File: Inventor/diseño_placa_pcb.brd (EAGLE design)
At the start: 100 x 80 mm, 14 parts, among them IC2 7805T

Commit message: pcb_design
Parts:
- removed JP1, JP3, JP4, JP5, JP6: (no value), jumper:JP1
- added VCC1: (no value), con-wago-500:W237-102
- moved X3 81.3 mm to (91.4, 64.8)
- moved X4 78.7 mm to (91.4, 54.6)
- moved VCC 77.8 mm to (88.9, 39.4)
- moved X1 77.6 mm to (12.7, 66.0), turned to 270 degrees
- moved X2 74.9 mm to (12.7, 55.9), turned to 270 degrees
- moved IC2 12.8 mm to (17.8, 21.6), turned to 0 degrees
- moved LEFT_MOTOR 10.5 mm to (34.3, 59.7)
- moved U$1 10.5 mm to (62.2, 16.5), turned to 0 degrees
- moved RIGHT_MOTOR 10.2 mm to (69.8, 59.7)
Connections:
- net N$15 renamed 3.3
- net N$16 renamed 1B_LEFT
- net N$17 renamed 1A_LEFT
- net N$18 renamed 2A_LEFT
- net N$19 renamed 2B_LEFT
- removed net N$6: IC2.2, LEFT_MOTOR.15, LEFT_MOTOR.9, RIGHT_MOTOR.15, RIGHT_MOTOR.9, U$1.GND@1, VCC.2
- new net DIR_RIGHT: RIGHT_MOTOR.8
- new net GND: RIGHT_MOTOR.15, RIGHT_MOTOR.9, U$1.GND@2, VCC.2
- new net N$20: LEFT_MOTOR.8, U$1.D14
- new net N$21: IC2.1, LEFT_MOTOR.16, VCC1.1
- new net S$1: IC2.2, LEFT_MOTOR.15, LEFT_MOTOR.9, VCC1.2
- new net STEP_RIGHT: RIGHT_MOTOR.7
- net N$10: no longer IC2.1, LEFT_MOTOR.16
- net N$12: now also LEFT_MOTOR.1
- net N$14: now also LEFT_MOTOR.7, U$1.D27; no longer LEFT_MOTOR.1
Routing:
- net N$6: track 208.3 -> 0.00 mm
- net N$2: track 141.8 -> 16.4 mm
- net GND: track 0.00 -> 114.8 mm
- net N$5: track 125.2 -> 16.1 mm
- net N$3: track 123.9 -> 15.3 mm
- net 2A_LEFT: track 120.7 -> 16.6 mm
- net 2B_LEFT: track 110.1 -> 17.9 mm
- net S$1: track 0.00 -> 84.1 mm
- net N$4: track 79.9 -> 14.5 mm
- net 1B_LEFT: track 76.5 -> 18.9 mm
- net STEP_RIGHT: track 0.00 -> 57.6 mm
- net DIR_RIGHT: track 0.00 -> 55.0 mm
- net N$21: track 0.00 -> 55.0 mm
- net 1A_LEFT: track 72.1 -> 17.6 mm
- net N$20: track 0.00 -> 52.3 mm
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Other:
- board text added: "GND"
- board text added: "V3.3"
- board text added: "VIN"
- board text added: "VMOT"
- board text added: "vcc"

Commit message: pcb
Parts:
- added U$2: HR911105A, HR911105A:RJ45
- moved U$1 14.5 mm to (48.3, 20.3)
- moved IC2 7.73 mm to (10.2, 22.9)
- moved X2 4.58 mm to (10.2, 52.1)
- moved VCC1 3.81 mm to (10.2, 40.6)
- moved X1 3.59 mm to (10.2, 63.5)
- moved VCC 2.84 mm to (91.4, 38.1)
- moved RIGHT_MOTOR 1.27 mm to (71.1, 59.7)
- moved X3 1.27 mm to (91.4, 66.0)
- moved X4 1.27 mm to (91.4, 53.3)
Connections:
- net 1A_LEFT renamed N$17
- net 1B_LEFT renamed N$16
- net 2A_LEFT renamed N$18
- net 2B_LEFT renamed N$19
- net 3.3 renamed N$15
- net GND renamed N$22
- removed net DIR_RIGHT: RIGHT_MOTOR.8
- removed net S$1: IC2.2, LEFT_MOTOR.15, LEFT_MOTOR.9, VCC1.2
- removed net STEP_RIGHT: RIGHT_MOTOR.7
- new net N$23: U$1.D16, U$2.RD-
- new net N$24: IC2.2, LEFT_MOTOR.15, LEFT_MOTOR.9, U$2.GND, VCC1.2
- new net N$25: U$1.D17, U$2.RD+
- new net N$26: U$1.D5, U$2.P5
- new net N$28: U$1.D18, U$2.P4
- new net N$29: U$1.D21, U$2.TD-
- new net N$30: U$1.D22, U$2.TD+
- new net N$6: RIGHT_MOTOR.8, U$1.D2
- new net N$9: RIGHT_MOTOR.7, U$1.D4
- net N$1: now also U$1.D34
- net N$13: now also U$2.NC
- net N$27: now also U$1.D35
- net N$7: now also U$1.D32
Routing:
- net N$24: track 0.00 -> 167.0 mm
- net N$13: track 32.9 -> 124.2 mm
- net N$9: track 0.00 -> 90.1 mm
- net N$6: track 0.00 -> 90.0 mm
- net N$15: track 149.9 -> 235.7 mm
- net S$1: track 84.1 -> 0.00 mm
- net STEP_RIGHT: track 57.6 -> 0.00 mm
- net DIR_RIGHT: track 55.0 -> 0.00 mm
- net N$27: track 30.4 -> 78.4 mm
- net N$7: track 33.6 -> 78.1 mm
- net N$25: track 0.00 -> 39.0 mm
- net N$23: track 0.00 -> 38.9 mm
- net N$26: track 0.00 -> 35.8 mm
- net N$1: track 23.9 -> 59.4 mm
- net N$28: track 0.00 -> 30.2 mm
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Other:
- board text removed: "GND"
- board text removed: "V3.3"
- board text removed: "VIN"
- board text removed: "VMOT"
- board text removed: "vcc"

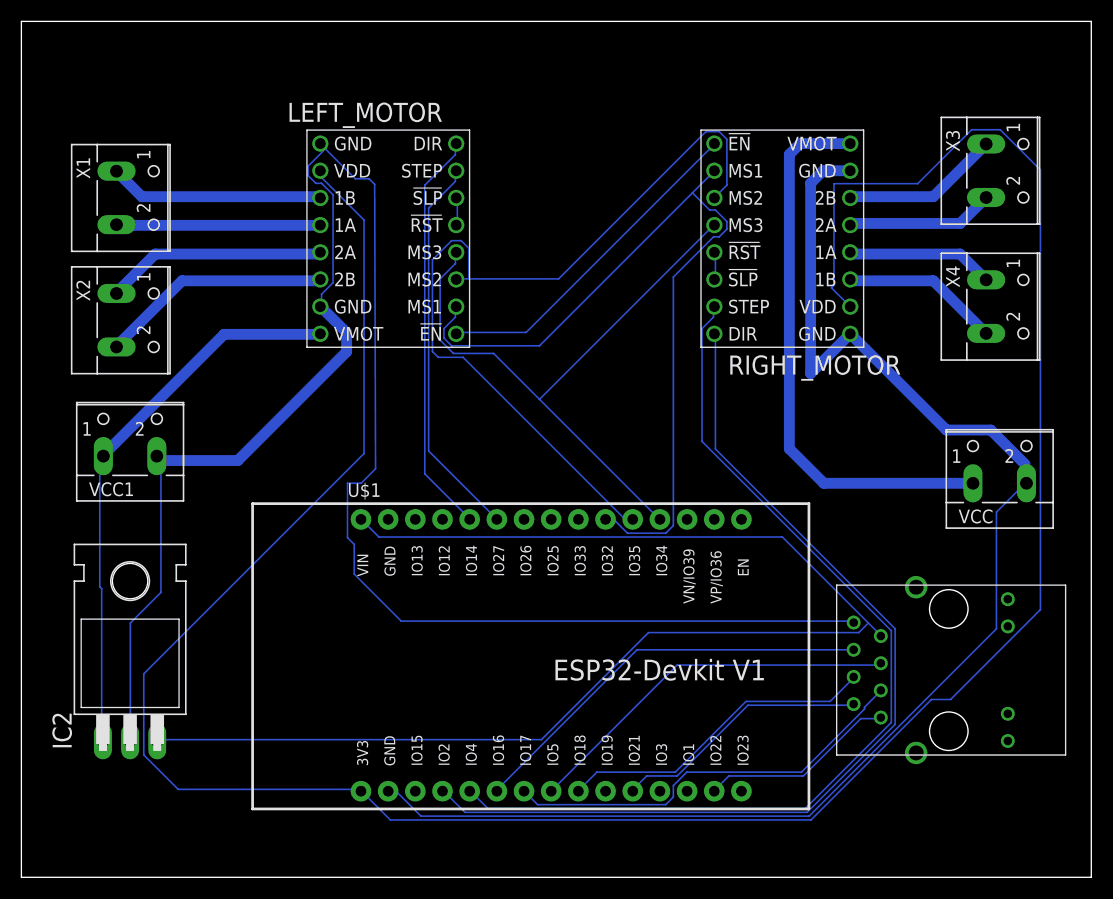
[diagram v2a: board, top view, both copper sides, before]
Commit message: otro diseño pcb
diseño considerando 1.2 mm
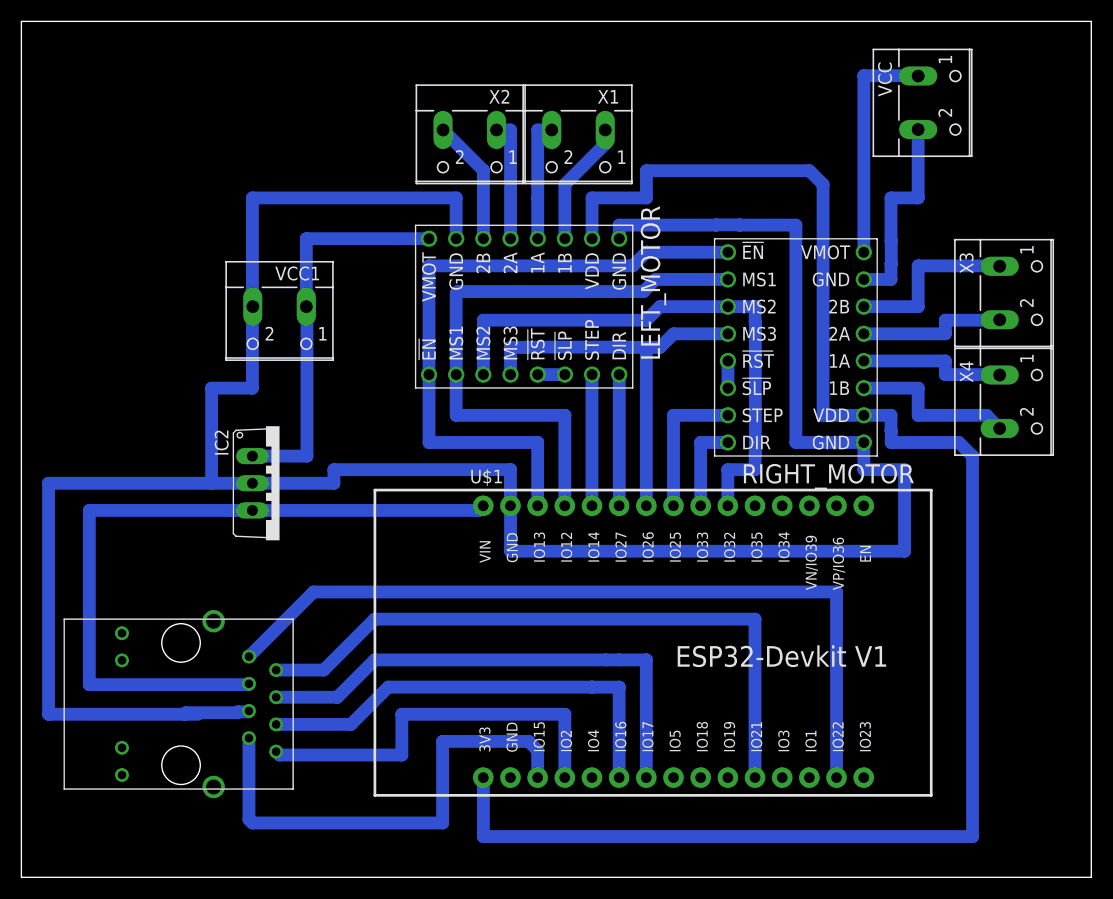
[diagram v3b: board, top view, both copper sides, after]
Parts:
- IC2: value 7805T -> 7805TV; device linear:TO220H -> linear:TO220V
- moved U$2 71.2 mm to (15.2, 16.5), turned to 180 degrees
- moved X1 42.2 mm to (52.1, 68.6), turned to 180 degrees
- moved X2 35.8 mm to (41.9, 68.6), turned to 180 degrees
- moved VCC 34.9 mm to (85.1, 72.4), turned to 270 degrees
- moved IC2 19.8 mm to (24.1, 36.8), turned to 270 degrees
- moved VCC1 18.1 mm to (24.1, 52.1), turned to 180 degrees
- moved LEFT_MOTOR 14.2 mm to (47.0, 53.3), turned to 90 degrees
- moved X3 11.5 mm to (92.7, 54.6)
- moved U$1 11.5 mm to (59.7, 21.6)
- moved RIGHT_MOTOR 10.2 mm to (72.4, 49.5)
- moved X4 8.98 mm to (92.7, 44.5)
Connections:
- net N$10 renamed VCC_2
- net N$15 renamed 3.3V
- net N$16 renamed 1B_L
- net N$17 renamed 1A_L
- net N$18 renamed 2A_L
- net N$19 renamed 2B_L
- net N$2 renamed 2B_R
- net N$21 renamed VCC
- net N$23 renamed RX
- net N$29 renamed SDA
- net N$3 renamed 2A_R
- net N$30 renamed SCL
- net N$4 renamed 1A_R
- net N$5 renamed 1B_R
- removed net N$1: LEFT_MOTOR.4, RIGHT_MOTOR.4, U$1.D34
- removed net N$12: LEFT_MOTOR.1, RIGHT_MOTOR.1
- removed net N$13: IC2.3, U$1.VIN, U$2.NC
- removed net N$14: LEFT_MOTOR.7, U$1.D27
- removed net N$20: LEFT_MOTOR.8, U$1.D14
- removed net N$22: RIGHT_MOTOR.15, RIGHT_MOTOR.9, U$1.GND@2, VCC.2
- removed net N$24: IC2.2, LEFT_MOTOR.15, LEFT_MOTOR.9, U$2.GND, VCC1.2
- removed net N$25: U$1.D17, U$2.RD+
- removed net N$26: U$1.D5, U$2.P5
- removed net N$27: LEFT_MOTOR.3, RIGHT_MOTOR.3, U$1.D35
- removed net N$28: U$1.D18, U$2.P4
- removed net N$6: RIGHT_MOTOR.8, U$1.D2
- removed net N$7: LEFT_MOTOR.2, RIGHT_MOTOR.2, U$1.D32
- removed net N$9: RIGHT_MOTOR.7, U$1.D4
- new net 5V: IC2.3, U$1.VIN, U$2.RD+
- new net DIR_L: LEFT_MOTOR.8, U$1.D27
- new net DIR_R: RIGHT_MOTOR.8, U$1.D33
- new net ENABLE: LEFT_MOTOR.1, RIGHT_MOTOR.1, U$1.D13
- new net GND: IC2.2, LEFT_MOTOR.15, LEFT_MOTOR.9, RIGHT_MOTOR.9, U$1.GND@1, U$2.P5, VCC1.2
- new net MS1: LEFT_MOTOR.2, RIGHT_MOTOR.2, U$1.D12
- new net MS2: LEFT_MOTOR.3, RIGHT_MOTOR.3, U$1.D32
- new net MS3: LEFT_MOTOR.4, RIGHT_MOTOR.4, U$1.D26
- new net RDY1: U$1.D15, U$2.NC
- new net S$1: RIGHT_MOTOR.15, VCC.2
- new net STEP_L: LEFT_MOTOR.7, U$1.D14
- new net STEP_R: RIGHT_MOTOR.7, U$1.D25
- new net TX: U$1.D17, U$2.P4
- new net VBB_EN: U$1.D2, U$2.GND
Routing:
- net GND: track 0.00 -> 242.5 mm
- net N$24: track 167.0 -> 0.00 mm
- net N$22: track 130.3 -> 0.00 mm
- net N$13: track 124.2 -> 0.00 mm
- net N$9: track 90.1 -> 0.00 mm
- net N$6: track 90.0 -> 0.00 mm
- net 3.3V: track 235.7 -> 153.9 mm
- net N$27: track 78.4 -> 0.00 mm
- net N$7: track 78.1 -> 0.00 mm
- net 5V: track 0.00 -> 68.3 mm
- net ENABLE: track 0.00 -> 61.1 mm
- net N$1: track 59.4 -> 0.00 mm
- net SCL: track 18.4 -> 74.8 mm
- net MS1: track 0.00 -> 56.0 mm
- net MS2: track 0.00 -> 52.2 mm
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
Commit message: diseño pcb
se realizó el diseño PCB considerando pistas de 1 mm
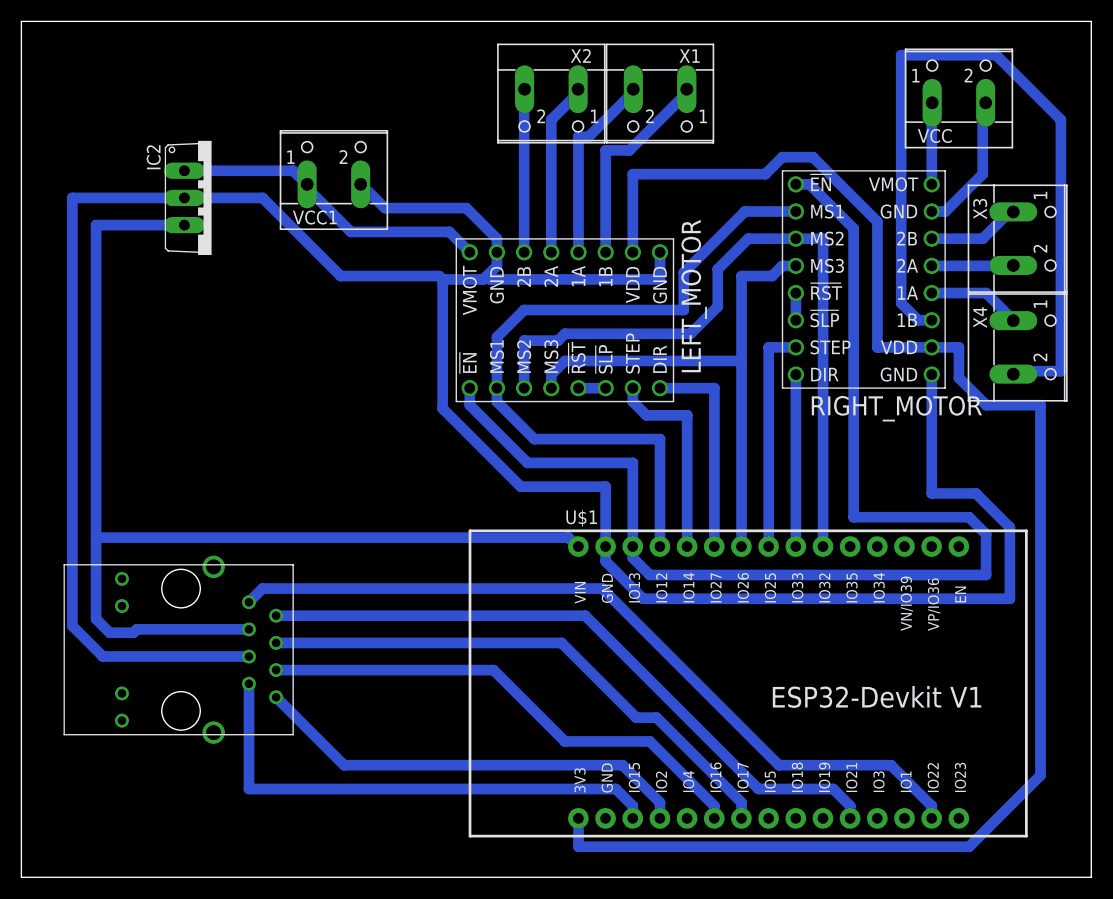
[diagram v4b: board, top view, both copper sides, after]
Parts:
- moved IC2 27.4 mm to (17.8, 63.5)
- moved VCC1 14.9 mm to (29.2, 66.0), turned to 0 degrees
- moved U$1 9.67 mm to (68.6, 17.8)
- moved RIGHT_MOTOR 8.98 mm to (78.7, 55.9)
- moved X2 8.52 mm to (49.5, 72.4)
- moved X1 8.52 mm to (59.7, 72.4)
- moved X3 5.24 mm to (94.0, 59.7)
- moved X4 5.24 mm to (94.0, 49.5)
- moved U$2 5.08 mm to (15.2, 21.6)
- moved LEFT_MOTOR 4.02 mm to (50.8, 52.1)
- moved VCC 2.84 mm to (87.6, 73.7), turned to 0 degrees
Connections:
- net 1A_L renamed N$21
- net 1A_R renamed N$4
- net 1B_L renamed N$19
- net 1B_R renamed N$20
- net 2A_L renamed N$22
- net 2A_R renamed N$18
- net 2B_L renamed N$23
- net 2B_R renamed N$17
- net 3.3V renamed N$15
- net 5V renamed N$13
- net DIR_L renamed N$9
- net DIR_R renamed N$11
- net ENABLE renamed N$1
- net GND renamed N$12
- net MS1 renamed N$2
- net MS2 renamed N$3
- net MS3 renamed N$5
- net RDY1 renamed N$32
- net RX renamed N$25
- net S$1 renamed N$14
- net SCL renamed N$28
- net SDA renamed N$29
- net STEP_L renamed N$7
- net STEP_R renamed N$10
- net TX renamed N$30
- net VBB_EN renamed N$31
- net VCC renamed N$26
- net VCC_2 renamed N$16
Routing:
- net N$20: track 15.7 -> 72.3 mm
- net N$1: track 61.1 -> 112.6 mm
- net N$13: track 68.3 -> 105.4 mm
- net N$3: track 52.2 -> 67.2 mm
- net N$16: track 21.6 -> 7.66 mm
- net N$5: track 38.2 -> 50.3 mm
- net N$2: track 56.0 -> 67.6 mm
- net N$19: track 11.8 -> 19.8 mm
- net N$17: track 16.5 -> 8.82 mm
- net N$10: track 13.5 -> 21.2 mm
- net N$11: track 8.46 -> 16.1 mm
- net N$9: track 12.3 -> 19.9 mm
- net N$7: track 12.3 -> 19.1 mm
- net N$21: track 11.5 -> 18.3 mm
- net N$26: track 36.9 -> 30.2 mm
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
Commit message: se crearon clases
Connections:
- net N$1 renamed ENABLE
- net N$10 renamed STEP_Y
- net N$11 renamed DIR_Y
- net N$12 renamed GND
- net N$13 renamed VCC_5V
- net N$15 renamed VCC_3.3
- net N$2 renamed MS1
- net N$25 renamed RX
- net N$26 renamed VIN
- net N$3 renamed MS2
- net N$30 renamed TX
- net N$31 renamed RDY1
- net N$32 renamed VBB_EN1
- net N$5 renamed MS3
- net N$7 renamed STEP_X
- net N$9 renamed DIR_X
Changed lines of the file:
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@@
 <wire x1="100" y1="80" x2="0" y2="80" width="0" layer="20"/>
 <wire x1="0" y1="80" x2="0" y2="0" width="0" layer="20"/>
+<dimension x1="100" y1="80" x2="100.33" y2="0" x3="132.008753125" y3="40.131353125" textsize="1.778" layer="16"/>
 </plain>
 <attributes>
@@
 <wire x1="54.61" y1="45.72" x2="52.07" y2="45.72" width="1" layer="16"/>
 </signal>
-<signal name="N$1">
+<signal name="ENABLE">
 <contactref element="LEFT_MOTOR" pad="1"/>
 <contactref element="RIGHT_MOTOR" pad="1"/>
@@
 <wire x1="57.15" y1="30.48" x2="57.14" y2="30.915" width="1" layer="16"/>
 </signal>
-<signal name="N$2">
+<signal name="MS1">
 <contactref element="LEFT_MOTOR" pad="2"/>
 <contactref element="RIGHT_MOTOR" pad="2"/>
@@
 <wire x1="44.45" y1="45.72" x2="44.45" y2="50.4825" width="1" layer="16"/>
 </signal>
-<signal name="N$3">
+<signal name="MS2">
 <contactref element="LEFT_MOTOR" pad="3"/>
 <contactref element="RIGHT_MOTOR" pad="3"/>
@@
 <wire x1="72.39" y1="59.69" x2="67.945" y2="59.69" width="1" layer="16"/>
 </signal>
-<signal name="N$5">
+<signal name="MS3">
 <contactref element="LEFT_MOTOR" pad="4"/>
 <contactref element="RIGHT_MOTOR" pad="4"/>
@@
 <wire x1="72.39" y1="54.61" x2="72.39" y2="52.07" width="1" layer="16"/>
 </signal>
-<signal name="N$7">
+<signal name="STEP_X">
 <contactref element="LEFT_MOTOR" pad="7"/>
 <contactref element="U$1" pad="D14"/>
@@
 <wire x1="62.23" y1="31.115" x2="62.22" y2="30.915" width="1" layer="16"/>
 </signal>
-<signal name="N$9">
+<signal name="DIR_X">
 <contactref element="LEFT_MOTOR" pad="8"/>
 <contactref element="U$1" pad="D27"/>
@@
 <wire x1="64.77" y1="31.115" x2="64.76" y2="30.915" width="1" layer="16"/>
 </signal>
-<signal name="N$10">
+<signal name="STEP_Y">
 <contactref element="U$1" pad="D25"/>
 <contactref element="RIGHT_MOTOR" pad="7"/>
@@
 <wire x1="69.85" y1="31.115" x2="69.84" y2="30.915" width="1" layer="16"/>
 </signal>
-<signal name="N$11">
+<signal name="DIR_Y">
 <contactref element="RIGHT_MOTOR" pad="8"/>
 <contactref element="U$1" pad="D33"/>
@@
 <wire x1="72.39" y1="31.115" x2="72.38" y2="30.915" width="1" layer="16"/>
 </signal>
-<signal name="N$12">
+<signal name="GND">
 <contactref element="U$1" pad="GND@1"/>
 <contactref element="IC2" pad="2"/>
@@
 <wire x1="39.0525" y1="56.1975" x2="39.37" y2="55.88" width="1" layer="16"/>
 </signal>
-<signal name="N$13">
+<signal name="VCC_5V">
 <contactref element="IC2" pad="3"/>
 <contactref element="U$1" pad="VIN"/>
@@
 <wire x1="51.7525" y1="31.115" x2="52.06" y2="30.915" width="1" layer="16"/>
 </signal>
-<signal name="N$15">
+<signal name="VCC_3.3">
 <contactref element="U$1" pad="3V3"/>
 <contactref element="RIGHT_MOTOR" pad="10"/>
@@
 <wire x1="46.99" y1="73.66" x2="47.03" y2="73.66" width="1" layer="16"/>
 </signal>
-<signal name="N$26">
+<signal name="VIN">
 <contactref element="IC2" pad="1"/>
 <contactref element="VCC1" pad="1"/>
@@
 <wire x1="77.47" y1="5.715" x2="77.46" y2="5.51" width="1" layer="16"/>
 </signal>
-<signal name="N$30">
+<signal name="TX">
 <contactref element="U$2" pad="P4"/>
 <contactref element="U$1" pad="D17"/>
@@
 <wire x1="67.31" y1="5.715" x2="67.3" y2="5.51" width="1" layer="16"/>
 </signal>
-<signal name="N$25">
+<signal name="RX">
 <contactref element="U$1" pad="D16"/>
 <contactref element="U$2" pad="RD-"/>
@@
 <wire x1="64.77" y1="5.715" x2="64.76" y2="5.51" width="1" layer="16"/>
 </signal>
-<signal name="N$31">
+<signal name="RDY1">
 <contactref element="U$2" pad="GND"/>
 <contactref element="U$1" pad="D2"/>
@@
 <wire x1="59.69" y1="5.715" x2="59.68" y2="5.51" width="1" layer="16"/>
 </signal>
-<signal name="N$32">
+<signal name="VBB_EN1">
 <contactref element="U$2" pad="NC"/>
 <contactref element="U$1" pad="D15"/>
